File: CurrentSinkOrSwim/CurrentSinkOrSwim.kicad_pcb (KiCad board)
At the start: 2 copper layers, 21 parts, among them K101 CONN_3, P101 CONN_2, P102 CONN_2, Q301 BUK7575, U201 LMV358, U401 LM2931ACDG

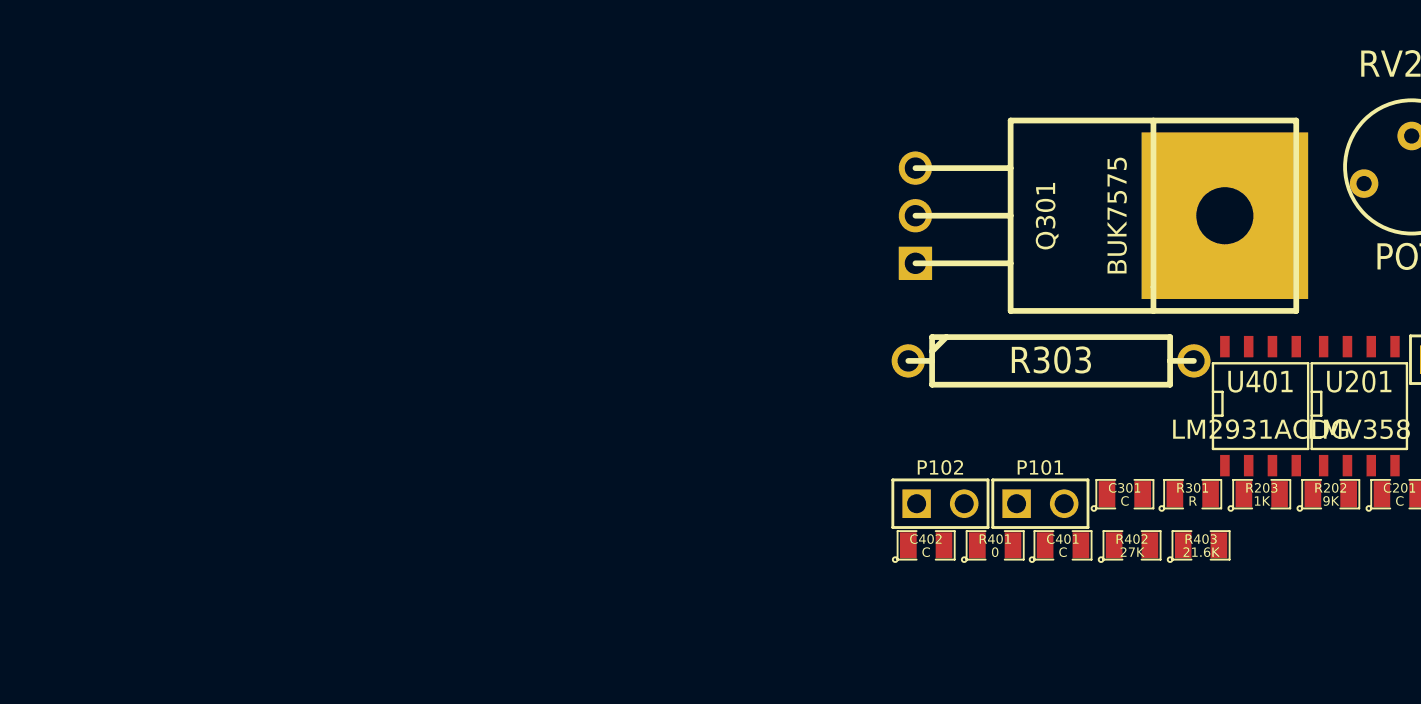
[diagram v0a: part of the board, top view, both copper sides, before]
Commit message: creado footprint heatsink
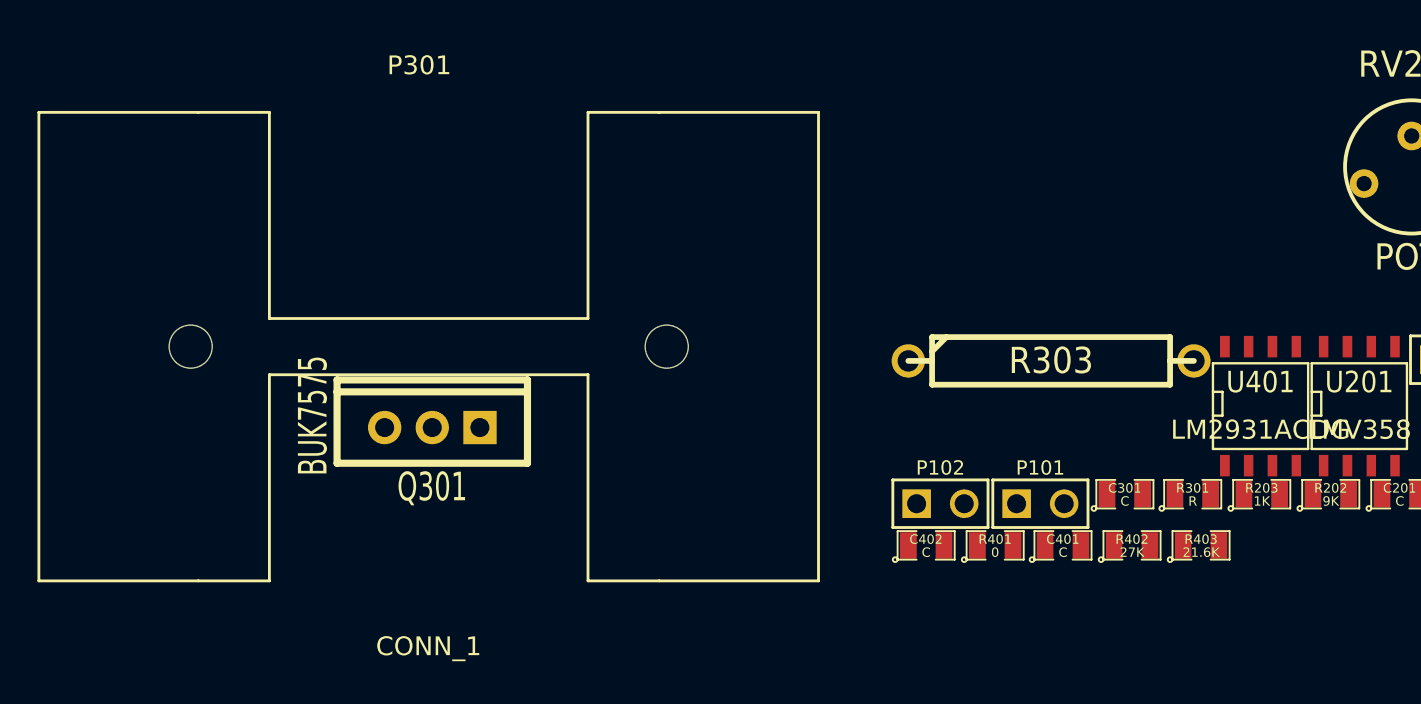
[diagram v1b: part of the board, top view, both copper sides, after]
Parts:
- added P301: CONN_1, Heat_Sink_FA-T220-38E, F.Cu at (77.6, 63.7)
- Q301: footprint TO220 -> TO220_VERT
- moved Q301 28.1 mm to (77.8, 68.0), turned to 90 degrees
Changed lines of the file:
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@@
     (tracks 0)
     (zones 0)
-    (modules 21)
+    (modules 22)
     (nets 15)
   )
@@
     (mod_text_size 1 1)
     (mod_text_width 0.15)
-    (pad_size 1.5 1.5)
-    (pad_drill 0.6)
+    (pad_size 2.3 2.3)
+    (pad_drill 2.3)
     (pad_to_mask_clearance 0)
     (aux_axis_origin 0 0)
-    (visible_elements FFFFFFBF)
+    (visible_elements 7FFFFFFF)
     (pcbplotparams
       (layerselection 3178497)
@@
   (net 5 GND)
   (net 6 N-0000011)
-  (net 7 N-0000013)
-  (net 8 N-0000014)
-  (net 9 N-0000015)
-  (net 10 N-0000016)
+  (net 7 N-0000014)
+  (net 8 N-0000015)
+  (net 9 N-0000016)
+  (net 10 N-0000017)
   (net 11 N-000003)
   (net 12 N-000006)
@@
     (add_net GND)
     (add_net N-0000011)
-    (add_net N-0000013)
     (add_net N-0000014)
     (add_net N-0000015)
     (add_net N-0000016)
+    (add_net N-0000017)
     (add_net N-000003)
     (add_net N-000006)
     (add_net N-000007)
     (add_net N-000008)
-  )
-  (module TO220 (layer F.Cu)
-    (at 103.5685 56.7055)
-    (descr "Transistor TO 220")
-    (tags "TR TO220 DEV")
-    (fp_text reference Q301 (at 6.985 0 90) (layer F.SilkS)
-      (effects (font (size 1.016 1.016) (thickness 0.2032)))
-    )
-    (fp_text value BUK7575 (at 10.795 0 90) (layer F.SilkS)
-      (effects (font (size 1.016 1.016) (thickness 0.2032)))
-    )
-    (fp_line (start 0 -2.54) (end 5.08 -2.54) (layer F.SilkS) (width 0.3048))
-    (fp_line (start 0 0) (end 5.08 0) (layer F.SilkS) (width 0.3048))
-    (fp_line (start 0 2.54) (end 5.08 2.54) (layer F.SilkS) (width 0.3048))
-    (fp_line (start 5.08 5.08) (end 20.32 5.08) (layer F.SilkS) (width 0.3048))
-    (fp_line (start 20.32 5.08) (end 20.32 -5.08) (layer F.SilkS) (width 0.3048))
-    (fp_line (start 20.32 -5.08) (end 5.08 -5.08) (layer F.SilkS) (width 0.3048))
-    (fp_line (start 5.08 -5.08) (end 5.08 5.08) (layer F.SilkS) (width 0.3048))
-    (fp_line (start 12.7 3.81) (end 12.7 -5.08) (layer F.SilkS) (width 0.3048))
-    (fp_line (start 12.7 3.81) (end 12.7 5.08) (layer F.SilkS) (width 0.3048))
-    (pad 1 thru_hole rect (at 0 2.54) (size 1.778 1.778) (drill 1.143)
-      (layers *.Cu *.Mask F.SilkS)
-    )
-    (pad 2 thru_hole circle (at 0 -2.54) (size 1.778 1.778) (drill 1.143)
-      (layers *.Cu *.Mask F.SilkS)
-    )
-    (pad 3 thru_hole circle (at 0 0) (size 1.778 1.778) (drill 1.143)
-      (layers *.Cu *.Mask F.SilkS)
-    )
-    (pad 4 thru_hole rect (at 16.51 0) (size 8.89 8.89) (drill 3.048)
-      (layers *.Cu *.SilkS *.Mask)
-    )
-    (model discret/to220_horiz.wrl
-      (at (xyz 0 0 0))
-      (scale (xyz 1 1 1))
-      (rotate (xyz 0 0 0))
-    )
   )
   (module SO8N (layer F.Cu)
@@
     (pad 5 smd rect (at 1.905 -3.175) (size 0.508 1.143)
       (layers F.Cu F.Paste F.Mask)
-      (net 9 N-0000015)
+      (net 9 N-0000016)
     )
     (pad 4 smd rect (at 1.905 3.175) (size 0.508 1.143)
       (layers F.Cu F.Paste F.Mask)
-      (net 10 N-0000016)
+      (net 10 N-0000017)
     )
     (pad 3 smd rect (at 0.635 3.175) (size 0.508 1.143)
@@
     (pad 6 smd rect (at 0.635 -3.175) (size 0.508 1.143)
       (layers F.Cu F.Paste F.Mask)
-      (net 8 N-0000014)
+      (net 8 N-0000015)
     )
     (pad 5 smd rect (at 1.905 -3.175) (size 0.508 1.143)
       (layers F.Cu F.Paste F.Mask)
-      (net 7 N-0000013)
+      (net 7 N-0000014)
     )
     (pad 4 smd rect (at 1.905 3.175) (size 0.508 1.143)
@@
     (pad 1 smd rect (at -0.9525 0) (size 0.889 1.397)
       (layers F.Cu F.Paste F.Mask)
-      (net 10 N-0000016)
+      (net 10 N-0000017)
     )
     (pad 2 smd rect (at 0.9525 0) (size 0.889 1.397)
@@
     (pad 2 smd rect (at 0.9525 0) (size 0.889 1.397)
       (layers F.Cu F.Paste F.Mask)
-      (net 10 N-0000016)
+      (net 10 N-0000017)
     )
     (model smd/chip_cms.wrl
@@
     (pad 1 smd rect (at -0.9525 0) (size 0.889 1.397)
       (layers F.Cu F.Paste F.Mask)
-      (net 9 N-0000015)
+      (net 9 N-0000016)
     )
     (pad 2 smd rect (at 0.9525 0) (size 0.889 1.397)
@@
     (pad 1 smd rect (at -0.9525 0) (size 0.889 1.397)
       (layers F.Cu F.Paste F.Mask)
-      (net 7 N-0000013)
+      (net 7 N-0000014)
     )
     (pad 2 smd rect (at 0.9525 0) (size 0.889 1.397)
@@
     (pad 3 thru_hole circle (at 2.54 1.27) (size 1.524 1.524) (drill 0.8128)
       (layers *.Cu *.Mask F.SilkS)
-      (net 7 N-0000013)
+      (net 7 N-0000014)
     )
     (model discret/adjustable_rx2.wrl
@@
     (pad 1 thru_hole circle (at -7.62 0) (size 1.778 1.778) (drill 1.143)
       (layers *.Cu *.Mask F.SilkS)
-      (net 8 N-0000014)
+      (net 8 N-0000015)
     )
     (pad 2 thru_hole circle (at 7.62 0) (size 1.778 1.778) (drill 1.143)
@@
     )
   )
+  (module Heat_Sink_FA-T220-38E (layer F.Cu)
+    (at 77.597 63.6905)
+    (fp_text reference P301 (at -0.5 -15) (layer F.SilkS)
+      (effects (font (size 1 1) (thickness 0.15)))
+    )
+    (fp_text value CONN_1 (at 0 16) (layer F.SilkS)
+      (effects (font (size 1 1) (thickness 0.15)))
+    )
+    (fp_line (start 12.3 12.5) (end 8.5 12.5) (layer F.SilkS) (width 0.15))
+    (fp_line (start -12.3 12.5) (end -8.5 12.5) (layer F.SilkS) (width 0.15))
+    (fp_line (start -8.5 -12.5) (end -12.3 -12.5) (layer F.SilkS) (width 0.15))
+    (fp_line (start 12.3 -12.5) (end 8.5 -12.5) (layer F.SilkS) (width 0.15))
+    (fp_line (start -8.5 12.5) (end -8.5 1.5) (layer F.SilkS) (width 0.15))
+    (fp_line (start -8.5 1.5) (end 8.5 1.5) (layer F.SilkS) (width 0.15))
+    (fp_line (start 8.5 1.5) (end 8.5 12.5) (layer F.SilkS) (width 0.15))
+    (fp_line (start -8.5 -1.5) (end 8.5 -1.5) (layer F.SilkS) (width 0.15))
+    (fp_line (start -8.5 -12.5) (end -8.5 -1.5) (layer F.SilkS) (width 0.15))
+    (fp_line (start 8.5 -12.5) (end 8.5 -1.5) (layer F.SilkS) (width 0.15))
+    (fp_line (start 20.8 -12.5) (end 12.3 -12.5) (layer F.SilkS) (width 0.15))
+    (fp_line (start -20.8 12.5) (end -12.3 12.5) (layer F.SilkS) (width 0.15))
+    (fp_line (start -20.8 -12.5) (end -12.3 -12.5) (layer F.SilkS) (width 0.15))
+    (fp_line (start 20.8 -12.5) (end 20.8 12.5) (layer F.SilkS) (width 0.15))
+    (fp_line (start 20.8 12.5) (end 12.3 12.5) (layer F.SilkS) (width 0.15))
+    (fp_line (start -20.8 12.5) (end -20.8 -12.5) (layer F.SilkS) (width 0.15))
+    (pad "" np_thru_hole circle (at -12.7 0) (size 2.3 2.3) (drill 2.3)
+      (layers *.Cu *.Mask F.SilkS)
+    )
+    (pad "" np_thru_hole circle (at 12.7 0) (size 2.3 2.3) (drill 2.3)
+      (layers *.Cu *.Mask F.SilkS)
+    )
+  )
+  (module TO220_VERT (layer F.Cu)
+    (at 77.7875 68.0085 90)
+    (descr "Regulateur TO220 serie LM78xx")
+    (tags "TR TO220")
+    (fp_text reference Q301 (at -3.175 0 180) (layer F.SilkS)
+      (effects (font (size 1.524 1.016) (thickness 0.2032)))
+    )
+    (fp_text value BUK7575 (at 0.635 -6.35 90) (layer F.SilkS)
+      (effects (font (size 1.524 1.016) (thickness 0.2032)))
+    )
+    (fp_line (start 1.905 -5.08) (end 2.54 -5.08) (layer F.SilkS) (width 0.381))
+    (fp_line (start 2.54 -5.08) (end 2.54 5.08) (layer F.SilkS) (width 0.381))
+    (fp_line (start 2.54 5.08) (end 1.905 5.08) (layer F.SilkS) (width 0.381))
+    (fp_line (start -1.905 -5.08) (end 1.905 -5.08) (layer F.SilkS) (width 0.381))
+    (fp_line (start 1.905 -5.08) (end 1.905 5.08) (layer F.SilkS) (width 0.381))
+    (fp_line (start 1.905 5.08) (end -1.905 5.08) (layer F.SilkS) (width 0.381))
+    (fp_line (start -1.905 5.08) (end -1.905 -5.08) (layer F.SilkS) (width 0.381))
+    (pad 2 thru_hole circle (at 0 -2.54 90) (size 1.778 1.778) (drill 1.016)
+      (layers *.Cu *.Mask F.SilkS)
+    )
+    (pad 3 thru_hole circle (at 0 0 90) (size 1.778 1.778) (drill 1.016)
+      (layers *.Cu *.Mask F.SilkS)
+    )
+    (pad 1 thru_hole rect (at 0 2.54 90) (size 1.778 1.778) (drill 1.016)
+      (layers *.Cu *.Mask F.SilkS)
+    )
+  )

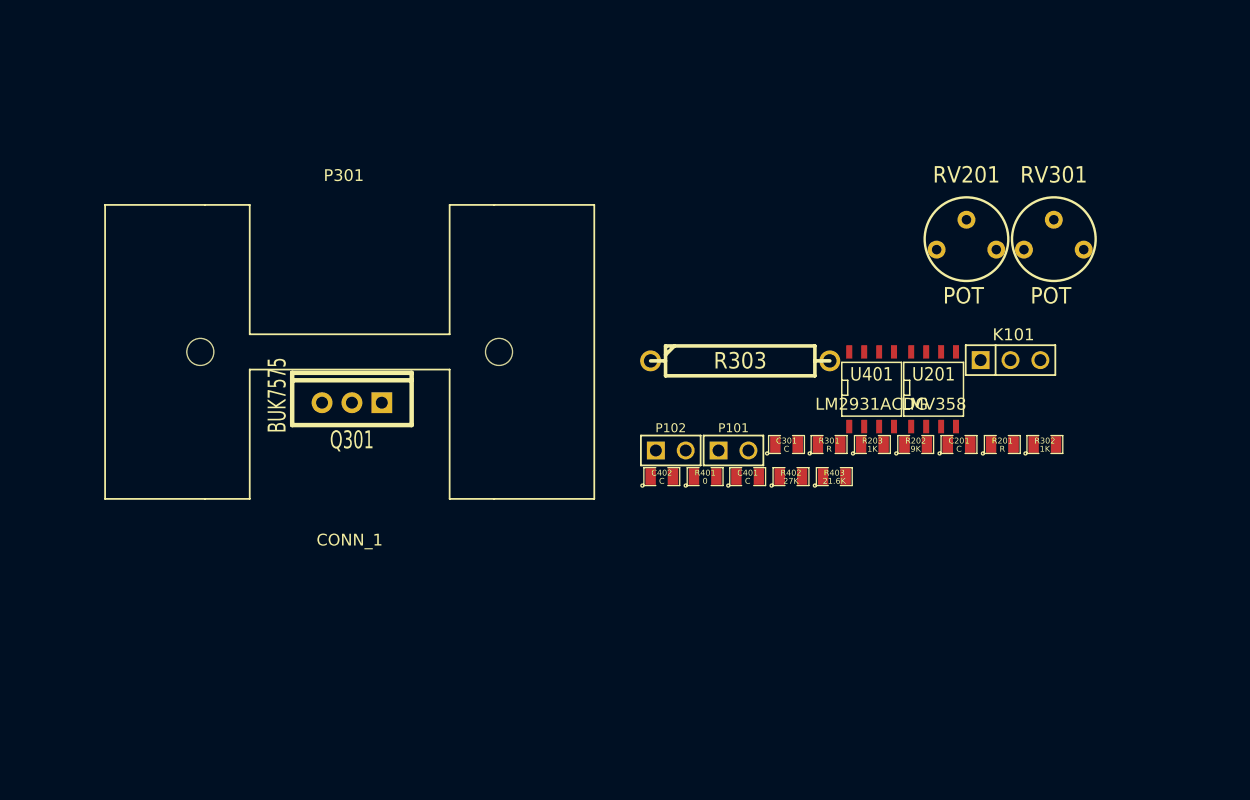
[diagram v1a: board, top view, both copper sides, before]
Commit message: Cambiados footprints del potenciometro
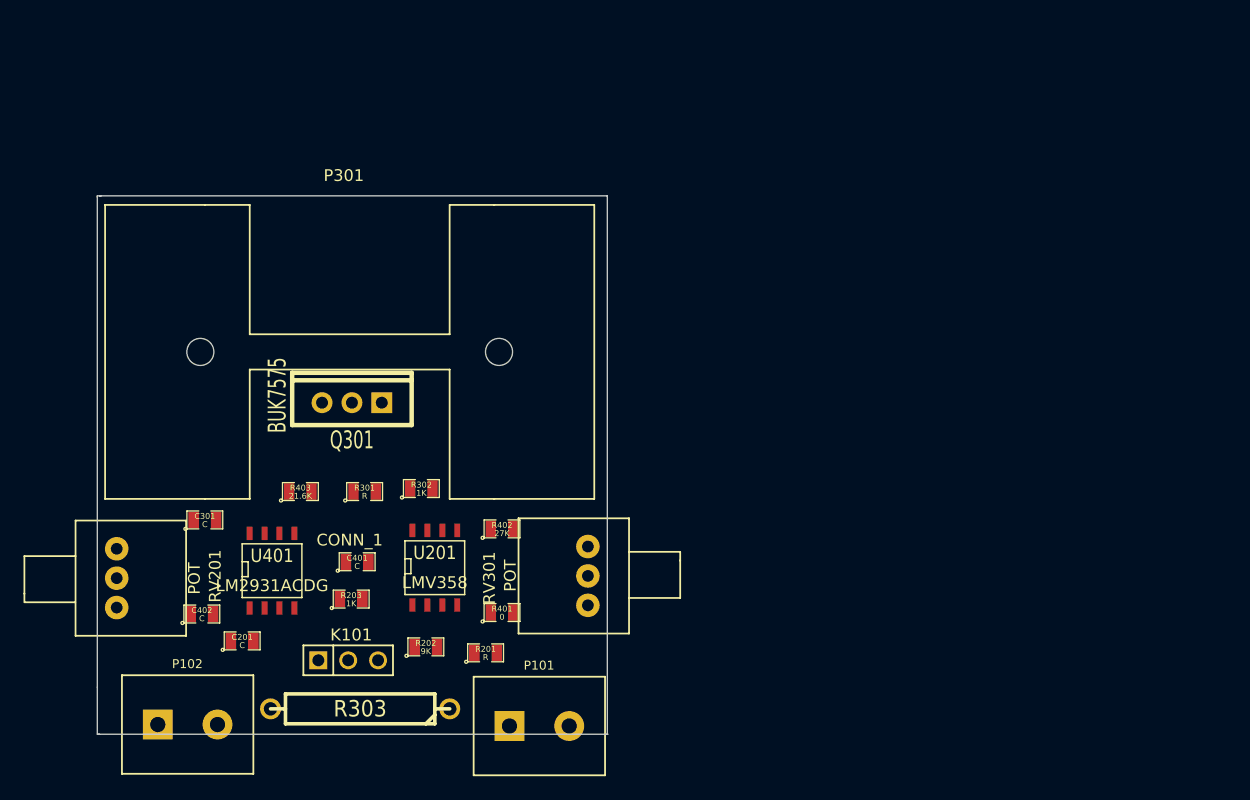
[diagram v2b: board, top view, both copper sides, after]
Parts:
- P101, P102: footprint PIN_ARRAY_2X1 -> Terminal_Block_200mil_5mm
- RV201, RV301: footprint RV2 -> ALPS_29_0001_Potenciometer_10k
- moved RV201 77.9 mm to (57.8, 82.9), turned to 270 degrees
- moved C201 63.2 mm to (68.5, 88.3)
- moved K101 61.8 mm to (77.5, 89.9)
- moved U401 53.3 mm to (71.0, 82.3)
- moved R302 53.2 mm to (83.7, 75.3)
- moved C301 49.9 mm to (65.3, 78.0)
- moved RV301 49.1 mm to (97.9, 82.7), turned to 90 degrees
- moved R201 47.4 mm to (89.2, 89.3)
- moved P102 47.2 mm to (63.8, 95.4)
- moved R203 46.2 mm to (77.7, 84.7)
- moved R403 45.4 mm to (73.4, 75.6)
- moved R202 45.1 mm to (84.1, 88.8)
- moved U201 45.1 mm to (84.8, 82.0)
- moved R303 43.8 mm to (78.5, 94.0), turned to 180 degrees
- moved C402 40.8 mm to (65.0, 86.0)
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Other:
- board outline added: 43.4 x 45.8 mm

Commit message: placing components in the PCB
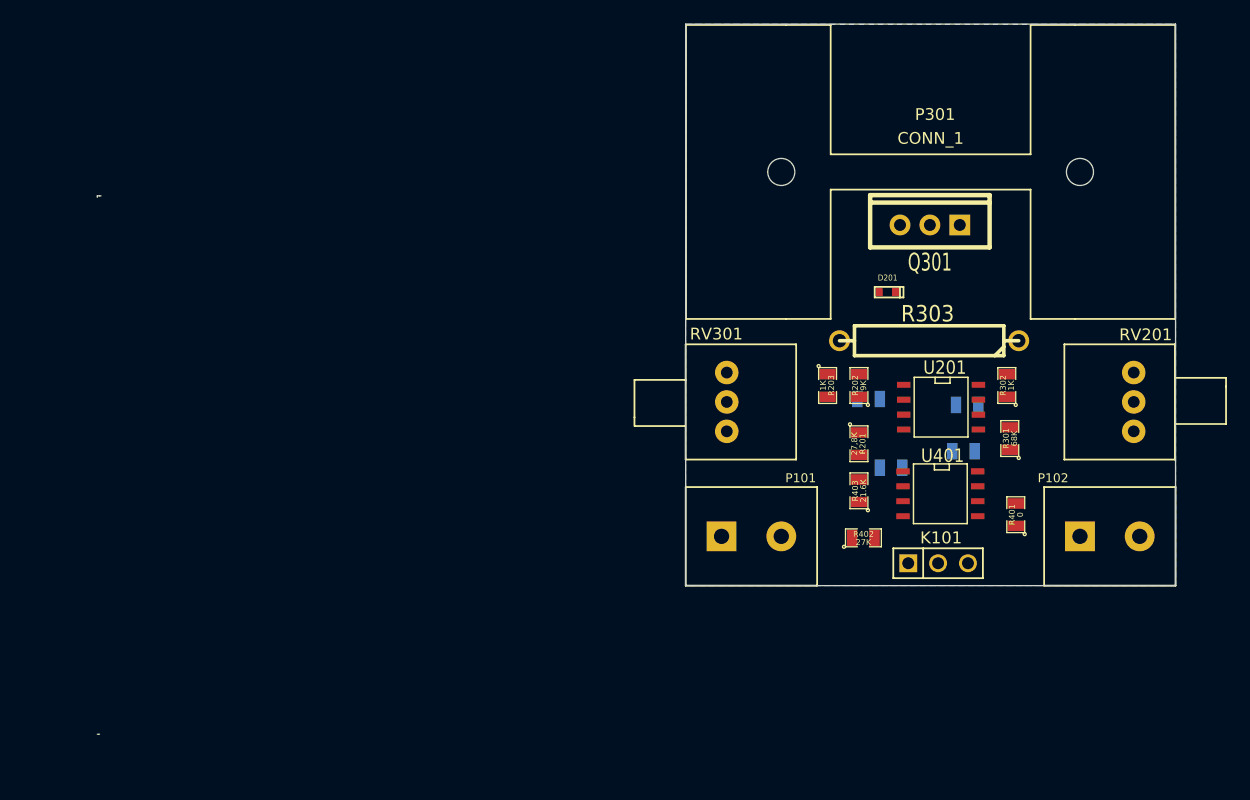
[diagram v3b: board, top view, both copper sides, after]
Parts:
- added D201: DIODE, DIODE_1N4148WT, F.Cu at (123.3, 58.6)
- C201, C301, C401, C402: moved to B.Cu
- Q301: footprint TO220_VERT -> BUK7575
- R201: value R -> 27,8K
- R301: value R -> 68K
- moved RV201 87.8 mm to (144.3, 67.9), turned to 90 degrees
- moved P102 80.0 mm to (142.2, 79.4)
- moved C402 66.2 mm to (129.8, 72.1)
- moved R303 57.6 mm to (126.9, 62.7)
- moved C301 57.4 mm to (121.7, 67.7)
- moved U401 57.2 mm to (127.8, 75.8), turned to 270 degrees
- moved C201 57.1 mm to (123.6, 73.5)
- moved R301 55.0 mm to (133.7, 71.1), turned to 90 degrees
- moved C401 53.6 mm to (130.1, 68.2)
- moved P301 51.7 mm to (127.0, 48.4)
- moved Q301 51.4 mm to (126.9, 52.9)
- moved K101 50.8 mm to (127.6, 81.7)
- moved R302 50.5 mm to (133.5, 66.5), turned to 90 degrees
- moved R403 47.5 mm to (120.9, 75.5), turned to 90 degrees
- moved U201 45.2 mm to (127.9, 68.4), turned to 270 degrees
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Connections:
- R201 pad 1: N-000008 (its old number) -> 2.7V
- R201 pad 2: GND -> N-000009
- R301 pad 1: N-0000014 -> 2.7V
- R301 pad 2: GND -> N-0000013
- R303 pad 1: N-0000015 -> N-0000014
- RV201 pad 2: 2.7V -> N-000009
- RV201 pad 3: N-000008 (its old number) -> GND
- RV301 pad 1: (no net) -> N-0000013
- RV301 pad 2: 2.7V -> GND
- RV301 pad 3: N-0000014 -> (no net)
- U201 pad 3: N-000008 (its old number) -> N-000009
- U201 pad 5: N-0000014 -> N-0000013
- U201 pad 6: N-0000015 -> N-0000014
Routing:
- added copper zone on B.Cu, net GND
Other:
- board size 43.4 x 45.8 mm -> 91.7 x 60.4 mm

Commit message: first layout session
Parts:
- moved RV201 34.6 mm to (109.7, 68.0), turned to 270 degrees
- moved RV301 34.0 mm to (143.6, 68.4), turned to 90 degrees
- moved C402 8.73 mm to (121.3, 70.2)
- moved C201 5.85 mm to (128.1, 69.7)
- moved C401 5.57 mm to (134.2, 72.0)
- moved R402 5.09 mm to (121.7, 74.4), turned to 270 degrees
- moved R201 3.90 mm to (117.3, 70.0)
- moved R403 2.47 mm to (121.7, 77.9), turned to 270 degrees
- moved R301 1.36 mm to (134.4, 69.8), turned to 180 degrees
- moved R401 0.97 mm to (134.7, 76.7)
- moved R303 0.95 mm to (126.8, 63.7)
- moved K101 0.25 mm to (127.6, 81.4)
- moved U201 0.06 mm to (127.8, 68.4)
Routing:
- net /Current Control/Current_Sink+: track 0.00 -> 62.1 mm
- net N-000003: track 0.00 -> 17.3 mm
- net /Power Regulation/Vin: track 0.00 -> 14.2 mm, vias 0 -> 1
- net GND: track 0.00 -> 6.75 mm, vias 0 -> 1
- net N-0000016: track 0.00 -> 3.75 mm
- net 2.7V: track 0.00 -> 3.14 mm
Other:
- net class Power added: clearance 0.3048, trace_width 0.6096, via_dia 1.143, via_drill 0.762
